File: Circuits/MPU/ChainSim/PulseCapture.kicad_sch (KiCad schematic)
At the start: 24 parts, among them U26 LT1715, U27 ADA4805-2ARMZ, U31 AD7984BRMZ

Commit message: sim snapshot
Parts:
- renumbered C115 to C35, C116 to C36, C117 to C37, C118 to C38, C119 to C39, C120 to C40, C121 to C41, C122 to C42, C123 to C43, C134 to C44, R159 to R50, R160 to R51, R161 to R52, R162 to R53, R163 to R54, R164 to R55, R165 to R56, R166 to R57, R167 to R58, R168 to R59, R169 to R60, U26 to U10, U27 to U11, U31 to U12

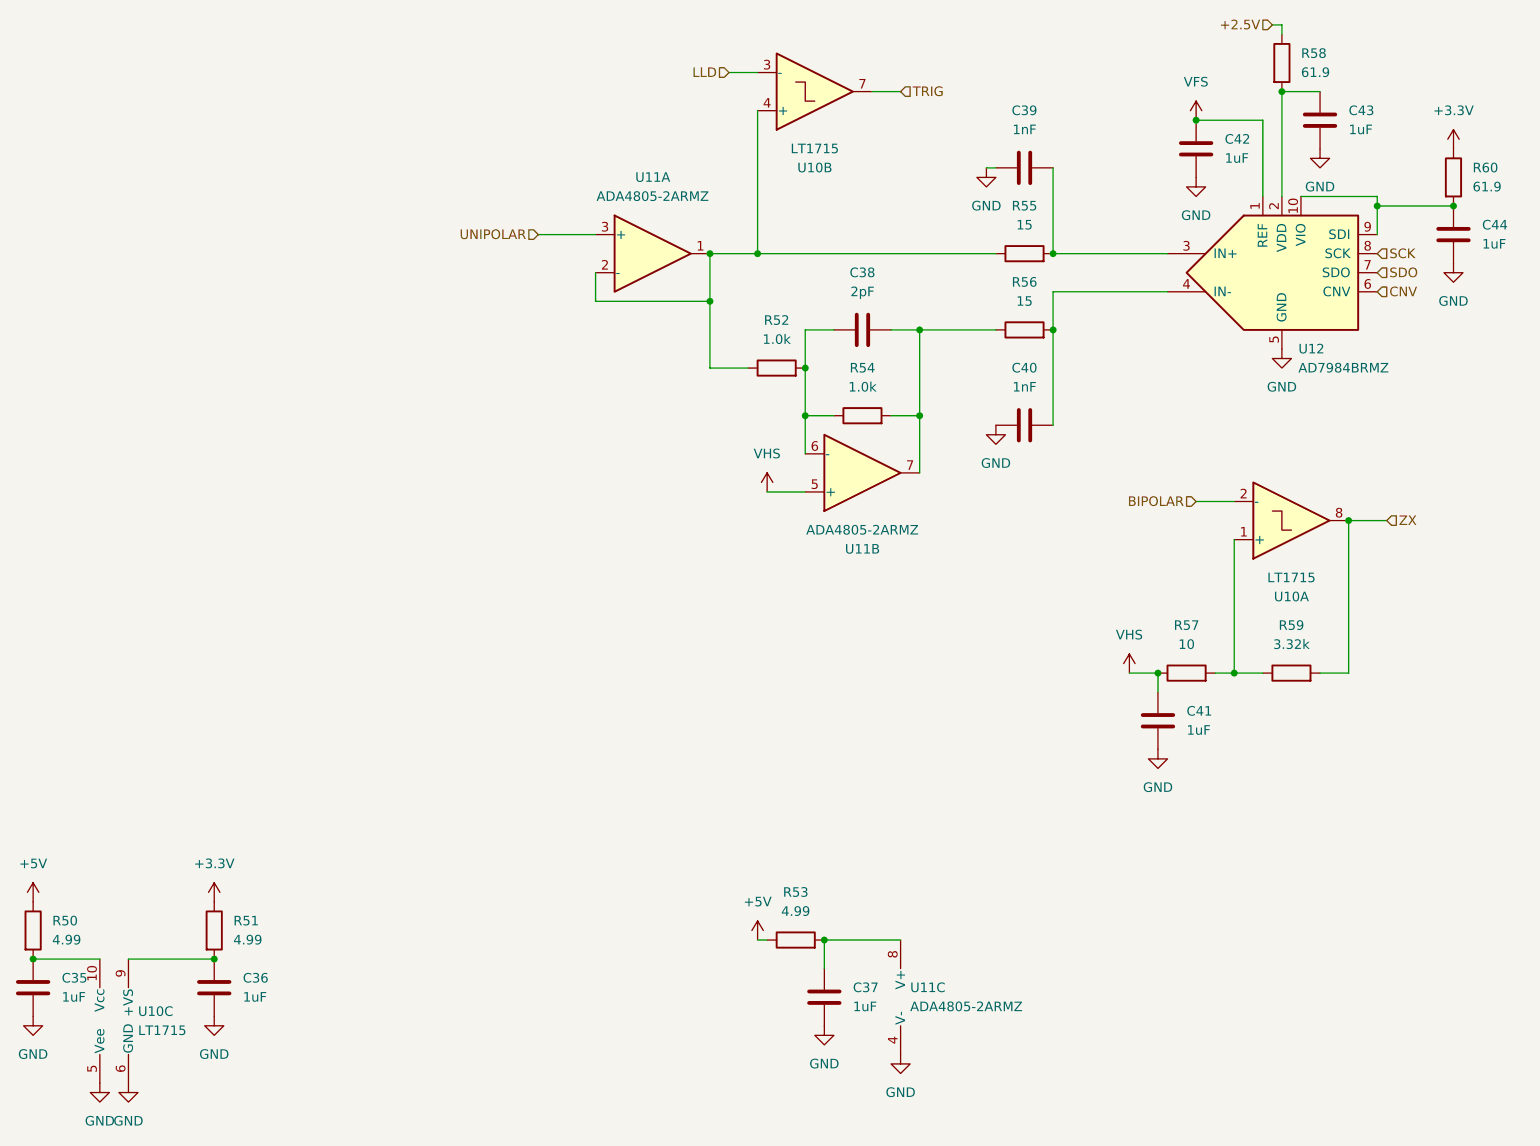
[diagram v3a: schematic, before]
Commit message: fix diode model
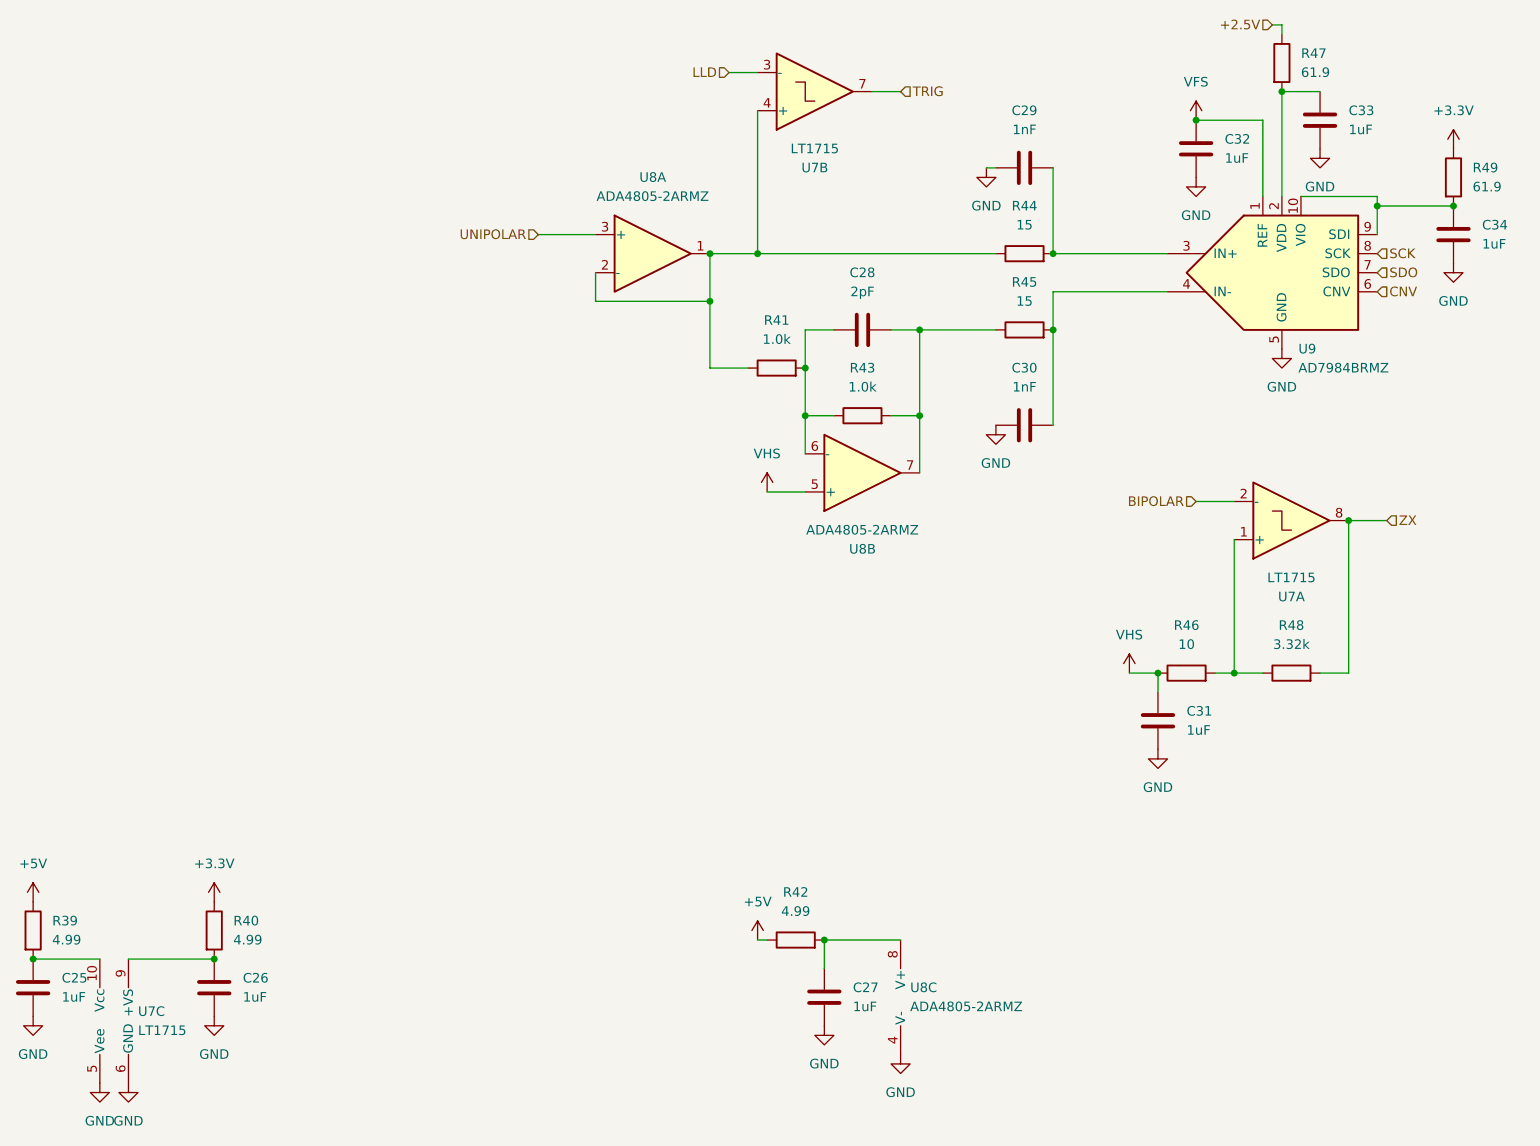
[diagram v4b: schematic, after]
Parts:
- renumbered C35 to C25, C36 to C26, C37 to C27, C38 to C28, C39 to C29, C40 to C30, C41 to C31, C42 to C32, C43 to C33, C44 to C34, R50 to R39, R51 to R40, R52 to R41, R53 to R42, R54 to R43, R55 to R44, R56 to R45, R57 to R46, R58 to R47, R59 to R48, R60 to R49, U10 to U7, U11 to U8, U12 to U9
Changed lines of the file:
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@@
 		(dnp no)
 		(fields_autoplaced yes)
-		(property "Reference" "#PWR073"
+		(property "Reference" "#PWR053"
 			(at 31.75 201.93 0)
 			(effects
@@
 		(dnp no)
 		(fields_autoplaced yes)
-		(property "Reference" "C43"
+		(property "Reference" "C33"
 			(at 198.12 66.04 0)
 			(effects
@@
 		(dnp no)
 		(fields_autoplaced yes)
-		(property "Reference" "C40"
+		(property "Reference" "C30"
 			(at 154.94 100.33 90)
 			(effects
@@
 		(on_board yes)
 		(dnp no)
-		(property "Reference" "U11"
+		(property "Reference" "U8"
 			(at 133.35 124.46 0)
 			(effects
@@
 		(dnp no)
 		(fields_autoplaced yes)
-		(property "Reference" "C37"
+		(property "Reference" "C27"
 			(at 132.08 182.88 0)
 			(effects
@@
 		(dnp no)
 		(fields_autoplaced yes)
-		(property "Reference" "C44"
+		(property "Reference" "C34"
 			(at 215.9 81.28 0)
 			(effects
@@
 		(dnp no)
 		(fields_autoplaced yes)
-		(property "Reference" "R56"
+		(property "Reference" "R45"
 			(at 154.94 88.9 90)
 			(effects
@@
 		(dnp no)
 		(fields_autoplaced yes)
-		(property "Reference" "#PWR084"
+		(property "Reference" "#PWR064"
 			(at 172.72 157.48 0)
 			(effects
@@
 		(dnp no)
 		(fields_autoplaced yes)
-		(property "Reference" "#PWR072"
+		(property "Reference" "#PWR052"
 			(at 22.86 193.04 0)
 			(effects
@@
 		(dnp no)
 		(fields_autoplaced yes)
-		(property "Reference" "U11"
+		(property "Reference" "U8"
 			(at 139.7 182.88 0)
 			(effects
@@
 		(dnp no)
 		(fields_autoplaced yes)
-		(property "Reference" "C38"
+		(property "Reference" "C28"
 			(at 133.35 87.63 90)
 			(effects
@@
 		(dnp no)
 		(fields_autoplaced yes)
-		(property "Reference" "#PWR075"
+		(property "Reference" "#PWR055"
 			(at 46.99 175.26 0)
 			(effects
@@
 		(dnp no)
 		(fields_autoplaced yes)
-		(property "Reference" "#PWR090"
+		(property "Reference" "#PWR070"
 			(at 212.09 92.71 0)
 			(effects
@@
 		(dnp no)
 		(fields_autoplaced yes)
-		(property "Reference" "U11"
+		(property "Reference" "U8"
 			(at 105.41 74.93 0)
 			(effects
@@
 		(dnp no)
 		(fields_autoplaced yes)
-		(property "Reference" "R53"
+		(property "Reference" "R42"
 			(at 124.46 170.18 90)
 			(effects
@@
 		(dnp no)
 		(fields_autoplaced yes)
-		(property "Reference" "#PWR071"
+		(property "Reference" "#PWR051"
 			(at 22.86 175.26 0)
 			(effects
@@
 		(dnp no)
 		(fields_autoplaced yes)
-		(property "Reference" "R55"
+		(property "Reference" "R44"
 			(at 154.94 78.74 90)
 			(effects
@@
 		(dnp no)
 		(fields_autoplaced yes)
-		(property "Reference" "#PWR086"
+		(property "Reference" "#PWR066"
 			(at 177.8 81.28 0)
 			(effects
@@
 		(dnp no)
 		(fields_autoplaced yes)
-		(property "Reference" "#PWR082"
+		(property "Reference" "#PWR062"
 			(at 151.13 114.3 0)
 			(effects
@@
 		(dnp no)
 		(fields_autoplaced yes)
-		(property "Reference" "#PWR089"
+		(property "Reference" "#PWR069"
 			(at 212.09 74.93 0)
 			(effects
@@
 		(dnp no)
 		(fields_autoplaced yes)
-		(property "Reference" "#PWR081"
+		(property "Reference" "#PWR061"
 			(at 149.86 80.01 0)
 			(effects
@@
 		(dnp no)
 		(fields_autoplaced yes)
-		(property "Reference" "R58"
+		(property "Reference" "R47"
 			(at 191.77 58.42 0)
 			(effects
@@
 		(dnp no)
 		(fields_autoplaced yes)
-		(property "Reference" "R57"
+		(property "Reference" "R46"
 			(at 176.53 134.62 90)
 			(effects
@@
 		(dnp no)
 		(fields_autoplaced yes)
-		(property "Reference" "#PWR078"
+		(property "Reference" "#PWR058"
 			(at 120.65 120.65 0)
 			(effects
@@
 		(dnp no)
 		(fields_autoplaced yes)
-		(property "Reference" "C36"
+		(property "Reference" "C26"
 			(at 50.8 181.61 0)
 			(effects
@@
 		(dnp no)
 		(fields_autoplaced yes)
-		(property "Reference" "C35"
+		(property "Reference" "C25"
 			(at 26.67 181.61 0)
 			(effects
@@
 		(on_board yes)
 		(dnp no)
-		(property "Reference" "U10"
+		(property "Reference" "U7"
 			(at 190.5 130.81 0)
 			(effects
@@
 		(dnp no)
 		(fields_autoplaced yes)
-		(property "Reference" "#PWR079"
+		(property "Reference" "#PWR059"
 			(at 128.27 194.31 0)
 			(effects
@@
 		(dnp no)
 		(fields_autoplaced yes)
-		(property "Reference" "C42"
+		(property "Reference" "C32"
 			(at 181.61 69.85 0)
 			(effects
@@
 		(dnp no)
 		(fields_autoplaced yes)
-		(property "Reference" "#PWR088"
+		(property "Reference" "#PWR068"
 			(at 194.31 77.47 0)
 			(effects
@@
 		(dnp no)
 		(fields_autoplaced yes)
-		(property "Reference" "C39"
+		(property "Reference" "C29"
 			(at 154.94 66.04 90)
 			(effects
@@
 		(dnp no)
 		(fields_autoplaced yes)
-		(property "Reference" "C41"
+		(property "Reference" "C31"
 			(at 176.53 146.05 0)
 			(effects
@@
 		(dnp no)
 		(fields_autoplaced yes)
-		(property "Reference" "R60"
+		(property "Reference" "R49"
 			(at 214.63 73.66 0)
 			(effects
@@
 		(dnp no)
 		(fields_autoplaced yes)
-		(property "Reference" "#PWR085"
+		(property "Reference" "#PWR065"
 			(at 177.8 71.12 0)
 			(effects
@@
 		(dnp no)
 		(fields_autoplaced yes)
-		(property "Reference" "R50"
+		(property "Reference" "R39"
 			(at 25.4 173.99 0)
 			(effects
@@
 		(dnp no)
 		(fields_autoplaced yes)
-		(property "Reference" "R52"
+		(property "Reference" "R41"
 			(at 121.92 93.98 90)
 			(effects
@@
 		(dnp no)
 		(fields_autoplaced yes)
-		(property "Reference" "R51"
+		(property "Reference" "R40"
 			(at 49.53 173.99 0)
 			(effects
@@
 		(dnp no)
 		(fields_autoplaced yes)
-		(property "Reference" "U12"
+		(property "Reference" "U9"
 			(at 191.4241 97.79 0)
 			(effects
@@
 		(dnp no)
 		(fields_autoplaced yes)
-		(property "Reference" "#PWR080"
+		(property "Reference" "#PWR060"
 			(at 138.43 198.12 0)
 			(effects
@@
 		(dnp no)
 		(fields_autoplaced yes)
-		(property "Reference" "R54"
+		(property "Reference" "R43"
 			(at 133.35 100.33 90)
 			(effects
@@
 		(dnp no)
 		(fields_autoplaced yes)
-		(property "Reference" "#PWR076"
+		(property "Reference" "#PWR056"
 			(at 46.99 193.04 0)
 			(effects
@@
 		(dnp no)
 		(fields_autoplaced yes)
-		(property "Reference" "#PWR087"
+		(property "Reference" "#PWR067"
 			(at 189.23 104.14 0)
 			(effects
@@
 		(dnp no)
 		(fields_autoplaced yes)
-		(property "Reference" "#PWR083"
+		(property "Reference" "#PWR063"
 			(at 168.91 144.78 0)
 			(effects
@@
 		(dnp no)
 		(fields_autoplaced yes)
-		(property "Reference" "#PWR077"
+		(property "Reference" "#PWR057"
 			(at 119.38 180.34 0)
 			(effects
@@
 		(on_board yes)
 		(dnp no)
-		(property "Reference" "U10"
+		(property "Reference" "U7"
 			(at 127 73.66 0)
 			(effects
@@
 		(dnp no)
 		(fields_autoplaced yes)
-		(property "Reference" "U10"
+		(property "Reference" "U7"
 			(at 36.83 186.055 0)
 			(effects
@@
 		(dnp no)
 		(fields_autoplaced yes)
-		(property "Reference" "R59"
+		(property "Reference" "R48"
 			(at 190.5 134.62 90)
 			(effects
@@
 		(dnp no)
 		(fields_autoplaced yes)
-		(property "Reference" "#PWR074"
+		(property "Reference" "#PWR054"
 			(at 35.56 201.93 0)
 			(effects
